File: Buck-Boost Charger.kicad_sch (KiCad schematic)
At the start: 46 parts, among them U11 BQ25756RRVR

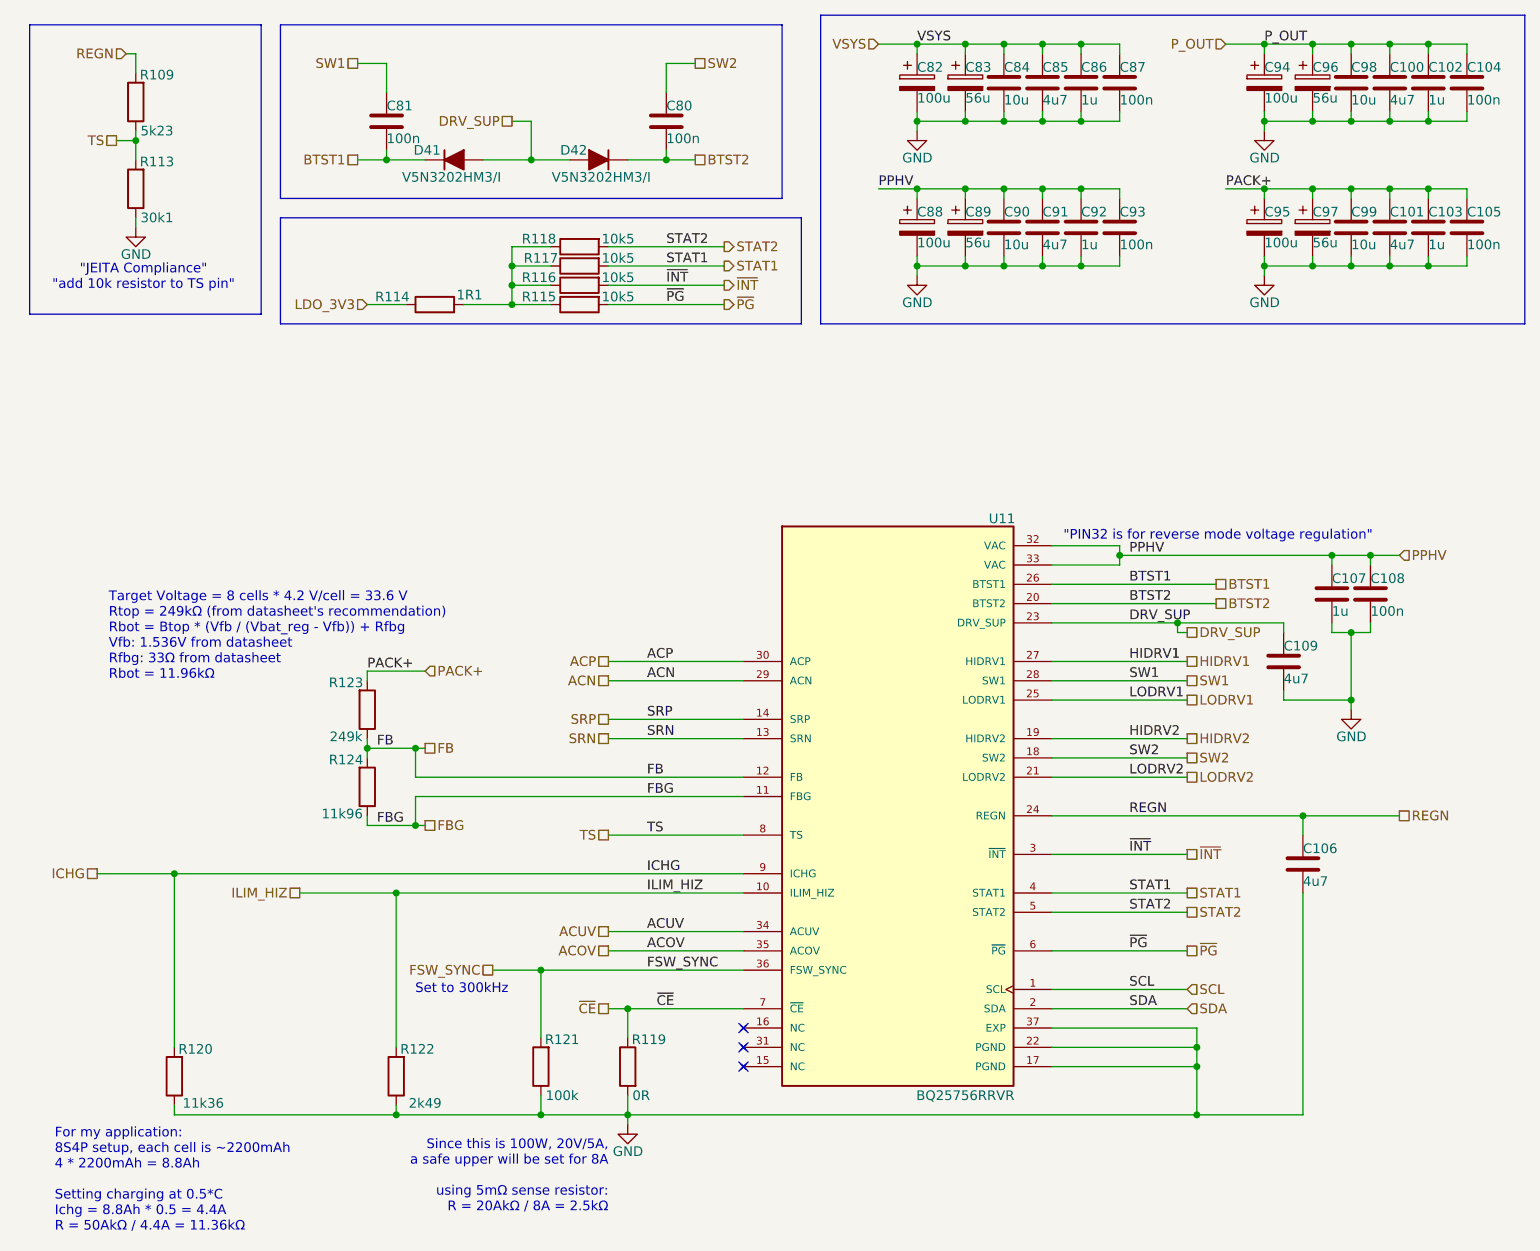
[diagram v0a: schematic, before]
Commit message: Fixed 5V Line
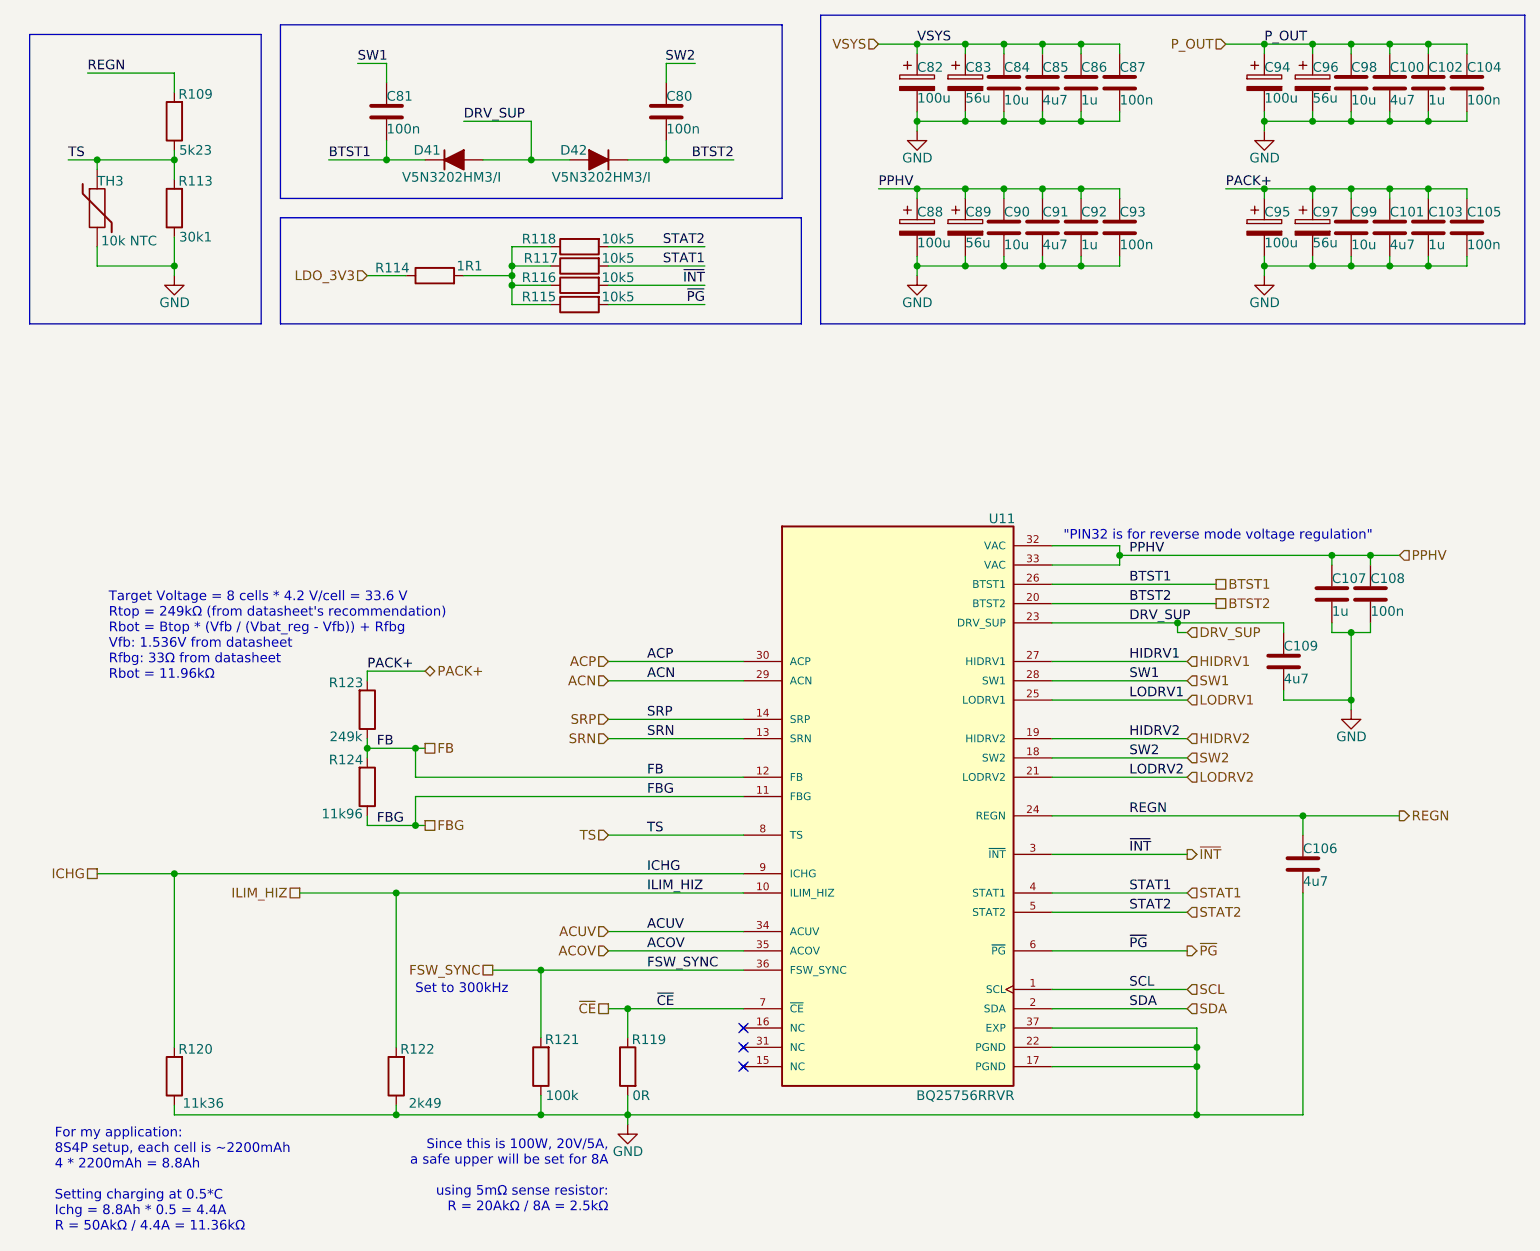
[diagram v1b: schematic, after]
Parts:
- added TH3: 10k NTC, symbol Device:Thermistor
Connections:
- net GND: now also TH3.2
- net TS: now also TH3.1
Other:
- note removed: ""JEITA Compliance" "add 10k resistor to TS pin""
- moved on the sheet: C80, C81, R109, R113, R114
